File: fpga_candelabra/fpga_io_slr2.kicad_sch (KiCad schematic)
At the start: 1 part, among them U1 XCVU13P-B2104

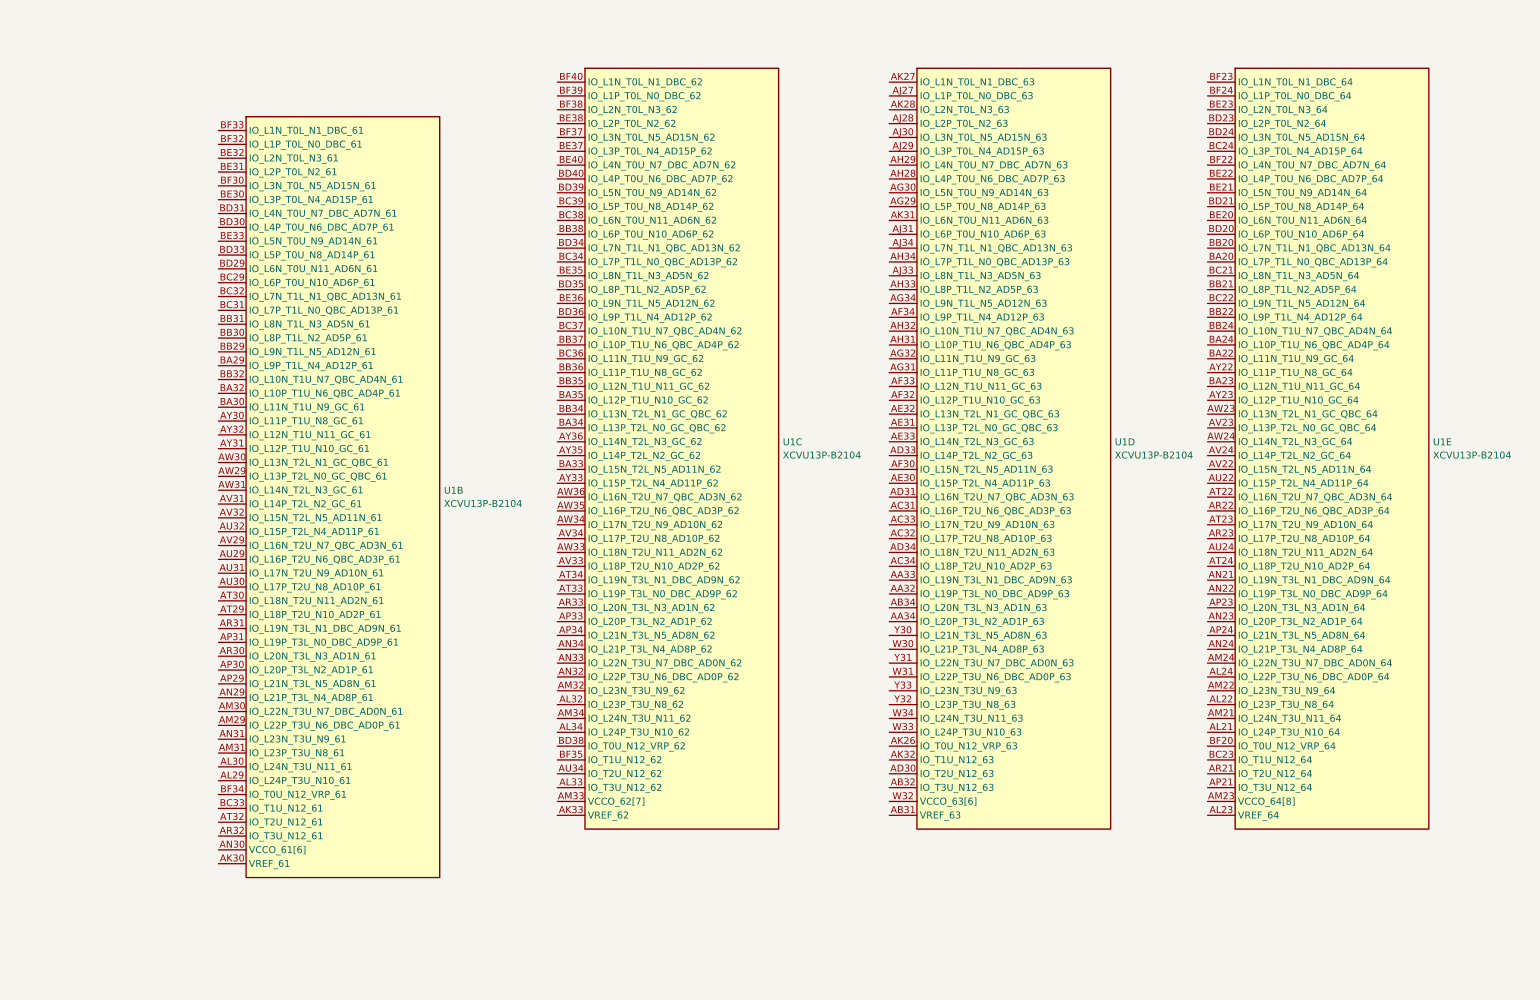
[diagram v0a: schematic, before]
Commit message: fpga_candelabra: reorganize fpga io and mgt by SLR
- Rename sch sheets
- Add prelimary DDR and PCIE Bank/Quad allocation

Signed-off-by: Yichuan Gao <gaoyichuan000@gmail.com>
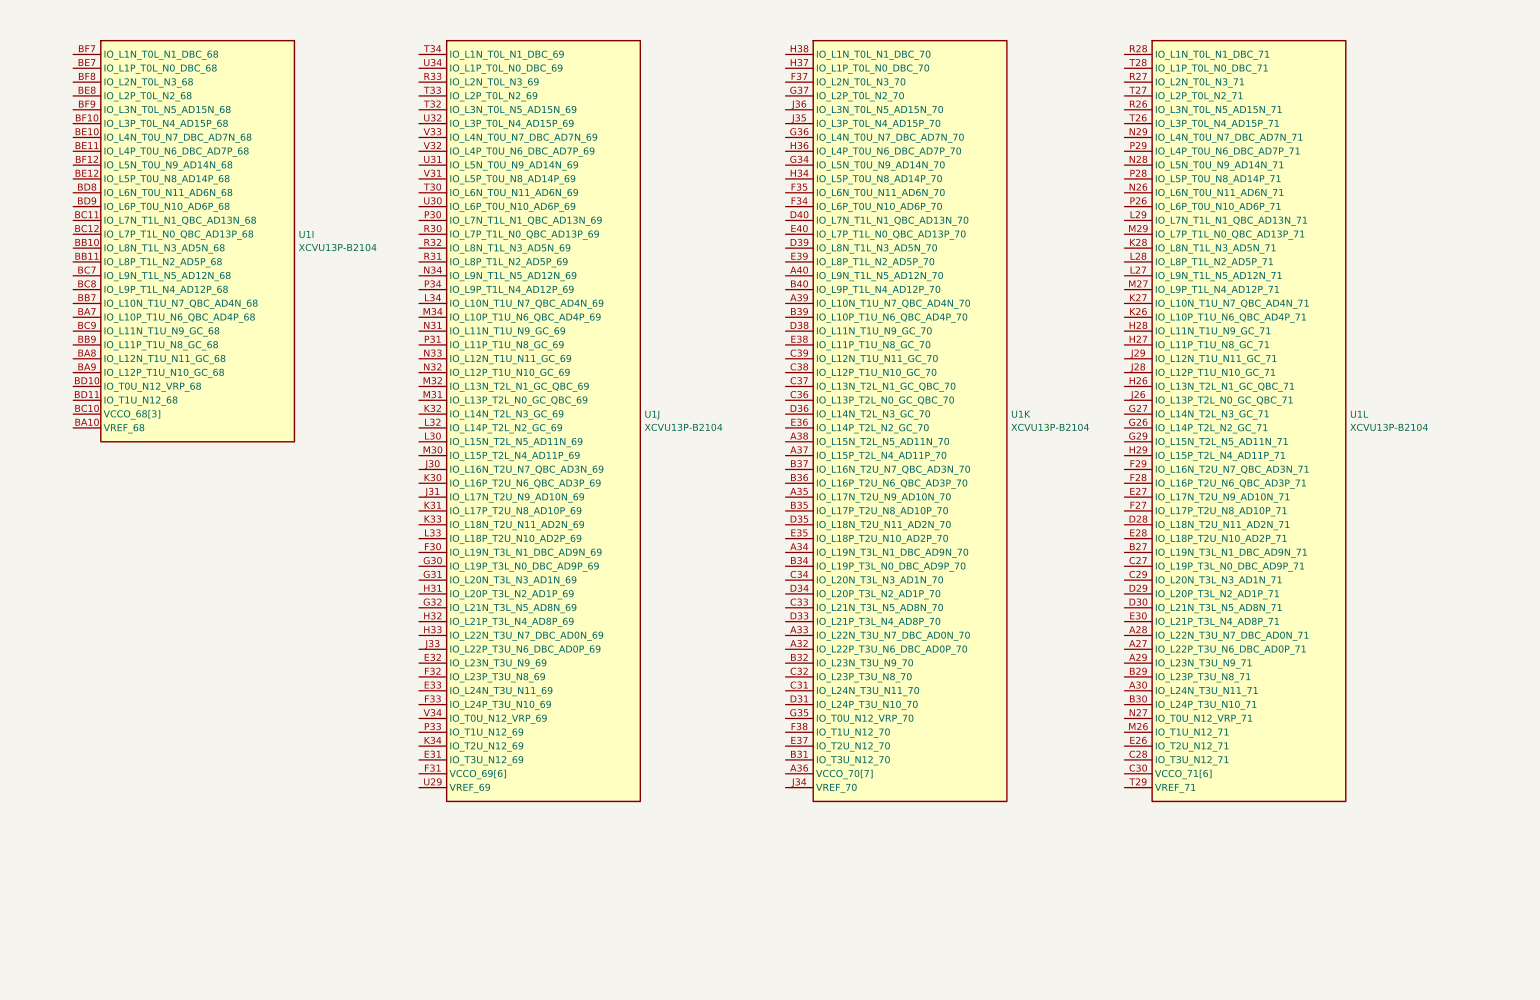
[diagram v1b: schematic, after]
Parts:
- removed U1: XCVU13P-B2104, CHIPSAlliance_Package_BGA:Xilinx_FHGB2104_VU13P_PkgLength, symbol CHIPSAlliance_FPGA_Xilinx_Virtex_UltraScale_Plus:XCVU13P-B2104
- added U1: XCVU13P-B2104, CHIPSAlliance_Package_BGA:Xilinx_FHGB2104_VU13P_PkgLength, symbol CHIPSAlliance_FPGA_Xilinx_Virtex_UltraScale_Plus:XCVU13P-B2104
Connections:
- new net: U1.C30 (VCCO_71[6]), U1.D27 (VCCO_71[6]), U1.G28 (VCCO_71[6]), U1.K29 (VCCO_71[6]), U1.L26 (VCCO_71[6]), U1.P27 (VCCO_71[6])
- new net: U1.F31 (VCCO_69[6]), U1.J32 (VCCO_69[6]), U1.M33 (VCCO_69[6]), U1.N30 (VCCO_69[6]), U1.R34 (VCCO_69[6]), U1.T31 (VCCO_69[6])
- new net: U1.BC10 (VCCO_68[3]), U1.BD7 (VCCO_68[3]), U1.BF11 (VCCO_68[3])
- new net: U1.A36 (VCCO_70[7]), U1.B33 (VCCO_70[7]), U1.C40 (VCCO_70[7]), U1.D37 (VCCO_70[7]), U1.E34 (VCCO_70[7]), U1.G38 (VCCO_70[7]), U1.H35 (VCCO_70[7])

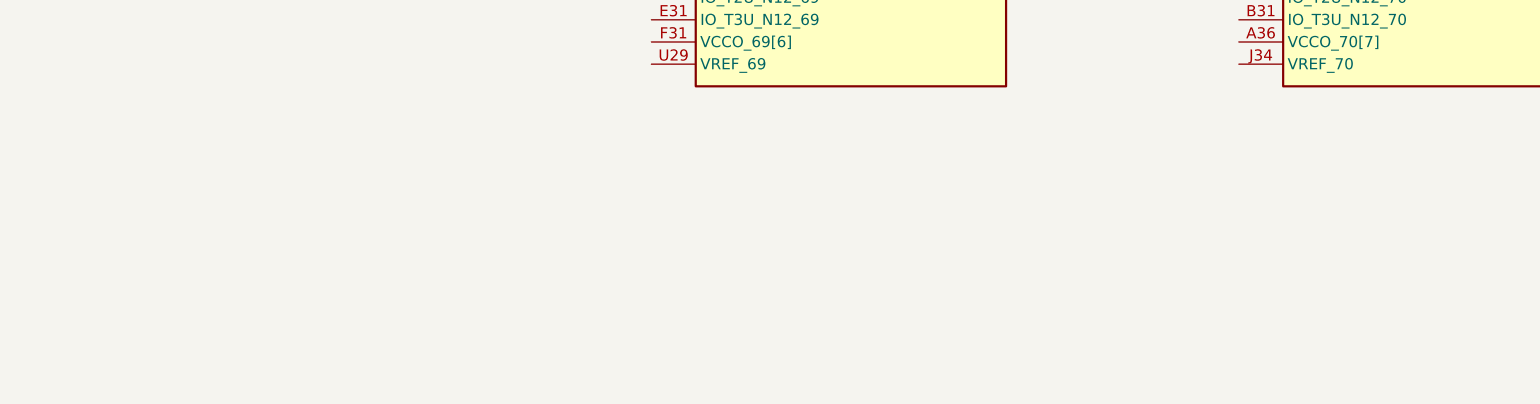
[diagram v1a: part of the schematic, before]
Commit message: candelabra: add i-pex extension ports, remove FMC1
* update bank/mgt allocation
* add basic pcb floorplanning

Signed-off-by: Yichuan Gao <gaoyichuan000@gmail.com>
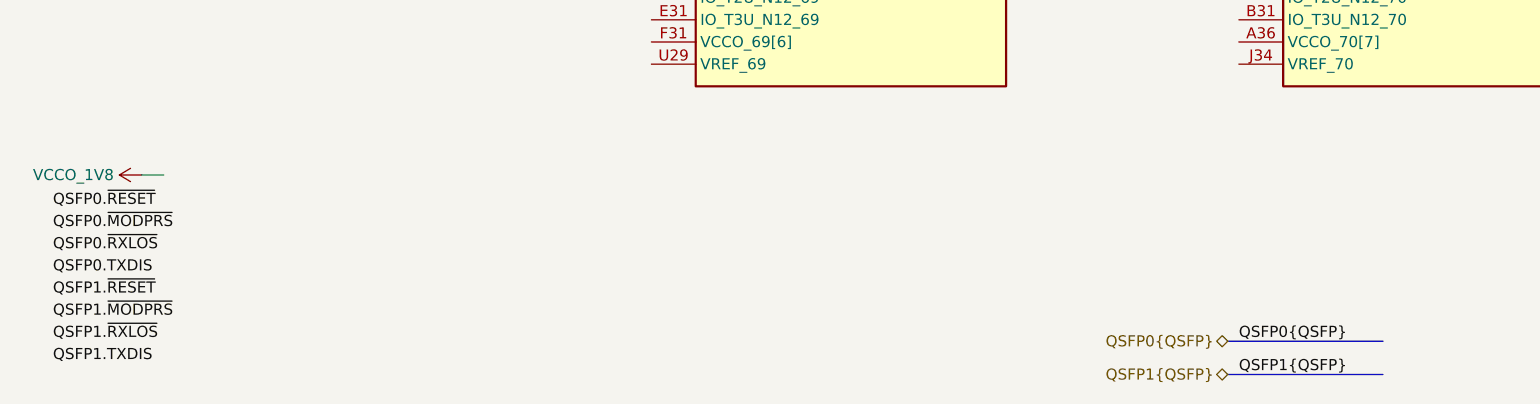
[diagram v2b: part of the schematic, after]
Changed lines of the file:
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@@
 	(generator_version "8.0")
 	(paper "A4")
+	(wire
+		(pts
+			(xy 30.48 170.18) (xy 33.02 170.18)
+		)
+		(stroke
+			(width 0)
+			(type default)
+		)
+	)
+	(bus
+		(pts
+			(xy 154.94 189.23) (xy 172.72 189.23)
+		)
+		(stroke
+			(width 0)
+			(type default)
+		)
+	)
+	(bus
+		(pts
+			(xy 154.94 193.04) (xy 172.72 193.04)
+		)
+		(stroke
+			(width 0)
+			(type default)
+		)
+	)
+	(label "QSFP0.TXDIS"
+		(at 20.32 181.61 0)
+		(fields_autoplaced yes)
+		(effects
+			(font
+				(size 1.27 1.27)
+			)
+			(justify left bottom)
+		)
+	)
+	(label "QSFP1.~{MODPRS}"
+		(at 20.32 186.69 0)
+		(fields_autoplaced yes)
+		(effects
+			(font
+				(size 1.27 1.27)
+			)
+			(justify left bottom)
+		)
+	)
+	(label "QSFP0.~{MODPRS}"
+		(at 20.32 176.53 0)
+		(fields_autoplaced yes)
+		(effects
+			(font
+				(size 1.27 1.27)
+			)
+			(justify left bottom)
+		)
+	)
+	(label "QSFP1.~{RXLOS}"
+		(at 20.32 189.23 0)
+		(fields_autoplaced yes)
+		(effects
+			(font
+				(size 1.27 1.27)
+			)
+			(justify left bottom)
+		)
+	)
+	(label "QSFP0.~{RESET}"
+		(at 20.32 173.99 0)
+		(fields_autoplaced yes)
+		(effects
+			(font
+				(size 1.27 1.27)
+			)
+			(justify left bottom)
+		)
+	)
+	(label "QSFP0{QSFP}"
+		(at 156.21 189.23 0)
+		(fields_autoplaced yes)
+		(effects
+			(font
+				(size 1.27 1.27)
+			)
+			(justify left bottom)
+		)
+	)
+	(label "QSFP1.TXDIS"
+		(at 20.32 191.77 0)
+		(fields_autoplaced yes)
+		(effects
+			(font
+				(size 1.27 1.27)
+			)
+			(justify left bottom)
+		)
+	)
+	(label "QSFP1.~{RESET}"
+		(at 20.32 184.15 0)
+		(fields_autoplaced yes)
+		(effects
+			(font
+				(size 1.27 1.27)
+			)
+			(justify left bottom)
+		)
+	)
+	(label "QSFP1{QSFP}"
+		(at 156.21 193.04 0)
+		(fields_autoplaced yes)
+		(effects
+			(font
+				(size 1.27 1.27)
+			)
+			(justify left bottom)
+		)
+	)
+	(label "QSFP0.~{RXLOS}"
+		(at 20.32 179.07 0)
+		(fields_autoplaced yes)
+		(effects
+			(font
+				(size 1.27 1.27)
+			)
+			(justify left bottom)
+		)
+	)
+	(hierarchical_label "QSFP0{QSFP}"
+		(shape bidirectional)
+		(at 154.94 189.23 180)
+		(fields_autoplaced yes)
+		(effects
+			(font
+				(size 1.27 1.27)
+			)
+			(justify right)
+		)
+	)
+	(hierarchical_label "QSFP1{QSFP}"
+		(shape bidirectional)
+		(at 154.94 193.04 180)
+		(fields_autoplaced yes)
+		(effects
+			(font
+				(size 1.27 1.27)
+			)
+			(justify right)
+		)
+	)
 	(symbol
 		(lib_id "CHIPSAlliance_FPGA_Xilinx_Virtex_UltraScale_Plus:XCVU13P-B2104")
@@
 				)
 			)
+		)
+	)
+	(symbol
+		(lib_id "power:+1V8")
+		(at 30.48 170.18 90)
+		(unit 1)
+		(exclude_from_sim no)
+		(in_bom yes)
+		(on_board yes)
+		(dnp no)
+		(fields_autoplaced yes)
+		(property "Reference" "#PWR0707"
+			(at 34.29 170.18 0)
+			(effects
+				(font
+					(size 1.27 1.27)
+				)
+				(hide yes)
+			)
+		)
+		(property "Value" "VCCO_1V8"
+			(at 27.3051 170.18 90)
+			(effects
+				(font
+					(size 1.27 1.27)
+				)
+				(justify left)
+			)
+		)
+		(property "Footprint" ""
+			(at 30.48 170.18 0)
+			(effects
+				(font
+					(size 1.27 1.27)
+				)
+				(hide yes)
+			)
+		)
+		(property "Datasheet" ""
+			(at 30.48 170.18 0)
+			(effects
+				(font
+					(size 1.27 1.27)
+				)
+				(hide yes)
+			)
+		)
+		(property "Description" "Power symbol creates a global label with name \"+1V8\""
+			(at 30.48 170.18 0)
+			(effects
+				(font
+					(size 1.27 1.27)
+				)
+				(hide yes)
+			)
+		)
+		(pin "1"
+		)
+		(instances
+			(project "fpga_candelabra"
+				(path "/01ed9e92-4e50-4b41-90dc-10444aaec5f7/048d3720-1b47-40c5-b543-cd301b5cf3fd"
+					(reference "#PWR0707")
+					(unit 1)
+				)
+			)

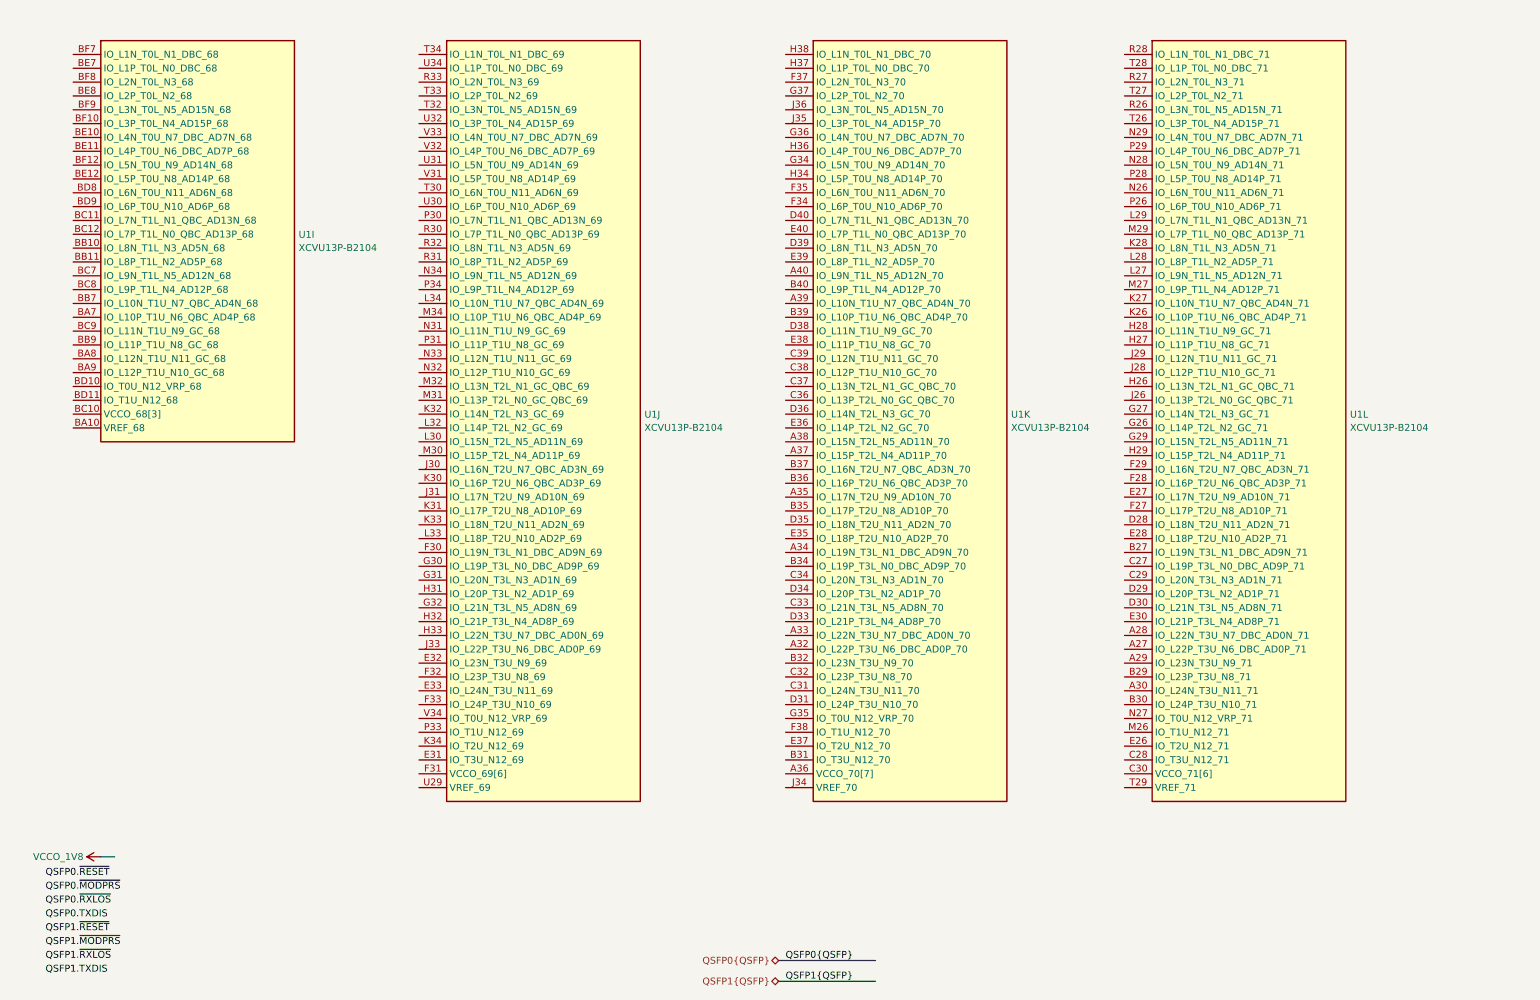
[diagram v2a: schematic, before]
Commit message: fpga_candelabra: major revision
* Finish DDR4 & QSFP+ & PCIe layout
* Change FMC to LPC
* Add mikroBUS extension
* 12V input & PDN updates
* FPGA config updates

Signed-off-by: Yichuan Gao <gaoyichuan000@gmail.com>
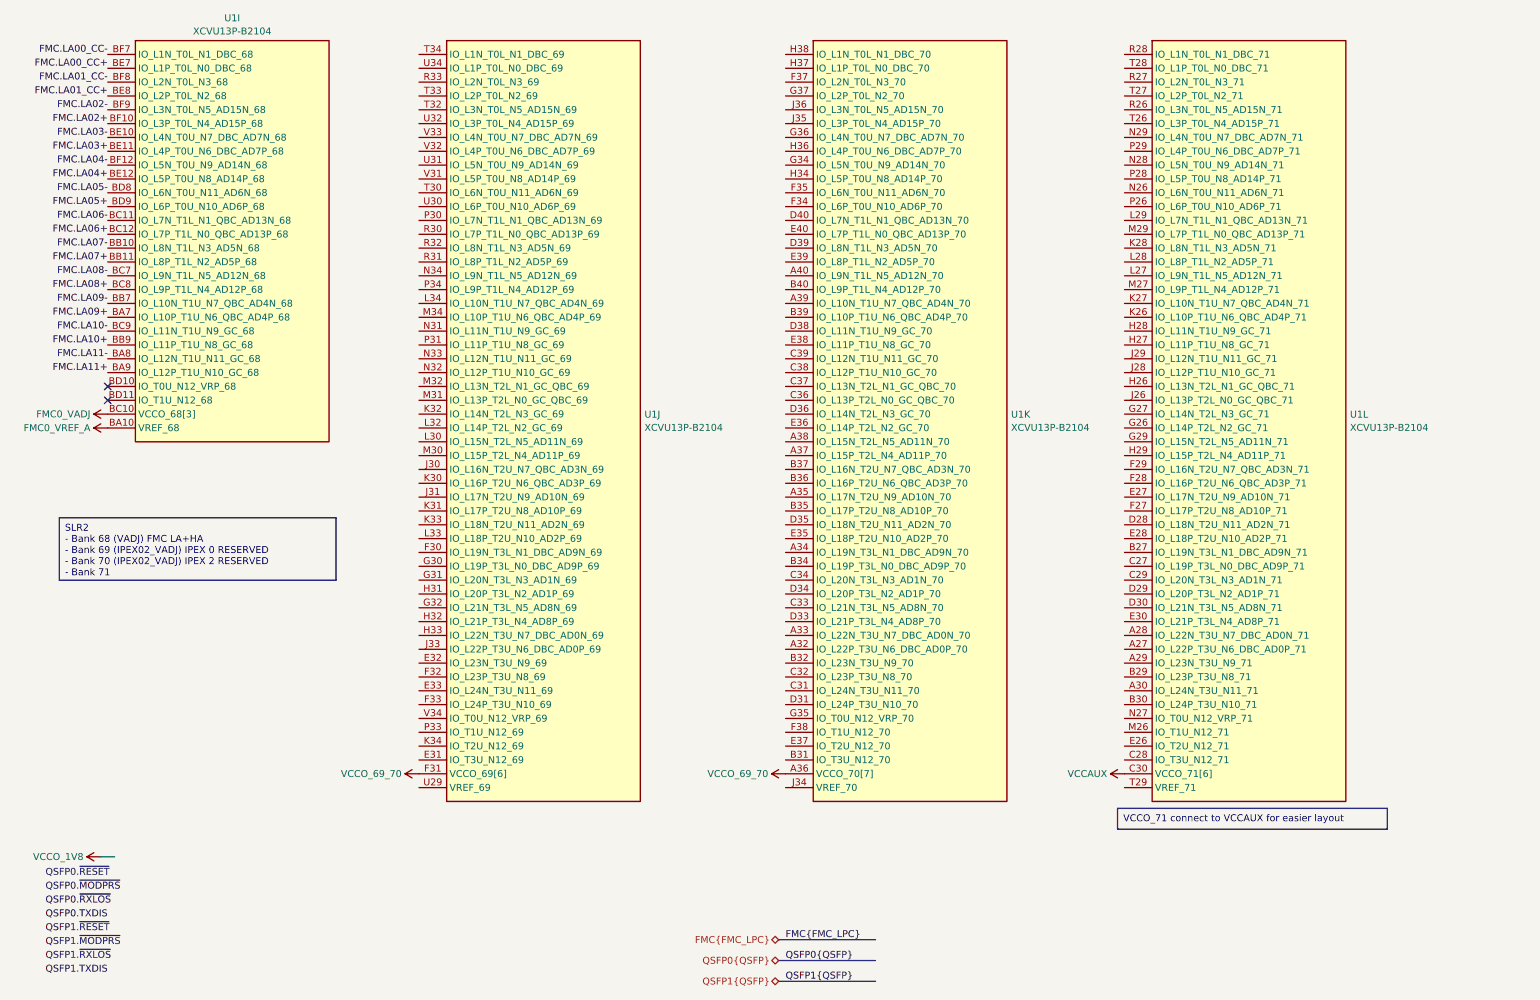
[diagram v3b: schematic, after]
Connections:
- net VCCAUX: now reaches U1.C30 (VCCO_71[6]), U1.D27 (VCCO_71[6]), U1.G28 (VCCO_71[6]), U1.K29 (VCCO_71[6]), U1.L26 (VCCO_71[6]), U1.P27 (VCCO_71[6])
- net VCCO_69_70: now reaches U1.F31 (VCCO_69[6]), U1.J32 (VCCO_69[6]), U1.M33 (VCCO_69[6]), U1.N30 (VCCO_69[6]), U1.R34 (VCCO_69[6]), U1.T31 (VCCO_69[6])
- net VCCO_69_70: now also U1.A36 (VCCO_70[7]), U1.B33 (VCCO_70[7]), U1.C40 (VCCO_70[7]), U1.D37 (VCCO_70[7]), U1.E34 (VCCO_70[7]), U1.G38 (VCCO_70[7]), U1.H35 (VCCO_70[7])
- net FMC0_VREF_A: now reaches U1.BA10 (VREF_68)
- net FMC.LA09+: now reaches U1.BA7 (IO_L10P_T1U_N6_QBC_AD4P_68)
- net FMC.LA11-: now reaches U1.BA8 (IO_L12N_T1U_N11_GC_68)
- net FMC.LA11+: now reaches U1.BA9 (IO_L12P_T1U_N10_GC_68)
- net FMC.LA07-: now reaches U1.BB10 (IO_L8N_T1L_N3_AD5N_68)
- net FMC.LA07+: now reaches U1.BB11 (IO_L8P_T1L_N2_AD5P_68)
- net FMC.LA09-: now reaches U1.BB7 (IO_L10N_T1U_N7_QBC_AD4N_68)
- net FMC.LA10+: now reaches U1.BB9 (IO_L11P_T1U_N8_GC_68)
- net FMC0_VADJ: now reaches U1.BC10 (VCCO_68[3]), U1.BD7 (VCCO_68[3]), U1.BF11 (VCCO_68[3])
- net FMC.LA06-: now reaches U1.BC11 (IO_L7N_T1L_N1_QBC_AD13N_68)
- net FMC.LA06+: now reaches U1.BC12 (IO_L7P_T1L_N0_QBC_AD13P_68)
- net FMC.LA08-: now reaches U1.BC7 (IO_L9N_T1L_N5_AD12N_68)
- net FMC.LA08+: now reaches U1.BC8 (IO_L9P_T1L_N4_AD12P_68)
- net FMC.LA10-: now reaches U1.BC9 (IO_L11N_T1U_N9_GC_68)
- net FMC.LA05-: now reaches U1.BD8 (IO_L6N_T0U_N11_AD6N_68)
- net FMC.LA05+: now reaches U1.BD9 (IO_L6P_T0U_N10_AD6P_68)
- net FMC.LA03-: now reaches U1.BE10 (IO_L4N_T0U_N7_DBC_AD7N_68)
- net FMC.LA03+: now reaches U1.BE11 (IO_L4P_T0U_N6_DBC_AD7P_68)
- net FMC.LA04+: now reaches U1.BE12 (IO_L5P_T0U_N8_AD14P_68)
- net FMC.LA00_CC+: now reaches U1.BE7 (IO_L1P_T0L_N0_DBC_68)
- net FMC.LA01_CC+: now reaches U1.BE8 (IO_L2P_T0L_N2_68)
- net FMC.LA02+: now reaches U1.BF10 (IO_L3P_T0L_N4_AD15P_68)
- net FMC.LA04-: now reaches U1.BF12 (IO_L5N_T0U_N9_AD14N_68)
- net FMC.LA00_CC-: now reaches U1.BF7 (IO_L1N_T0L_N1_DBC_68)
- net FMC.LA01_CC-: now reaches U1.BF8 (IO_L2N_T0L_N3_68)
- net FMC.LA02-: now reaches U1.BF9 (IO_L3N_T0L_N5_AD15N_68)
- no-connect marks 0 -> 2
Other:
- moved on the sheet: U1I
